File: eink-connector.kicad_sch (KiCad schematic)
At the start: 18 parts, among them J4 FFC-FPC_1X24_PIN, Q1 Si1308EDL

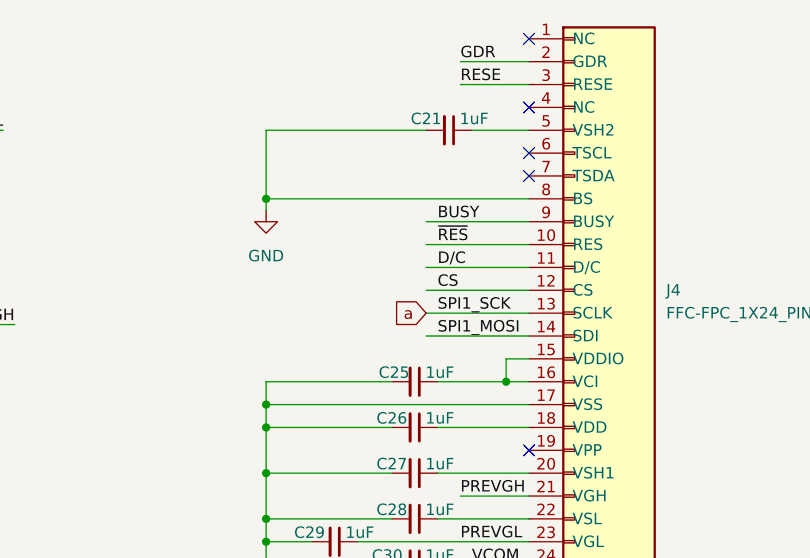
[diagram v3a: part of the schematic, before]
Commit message: Cleaned up local vs. global net labels
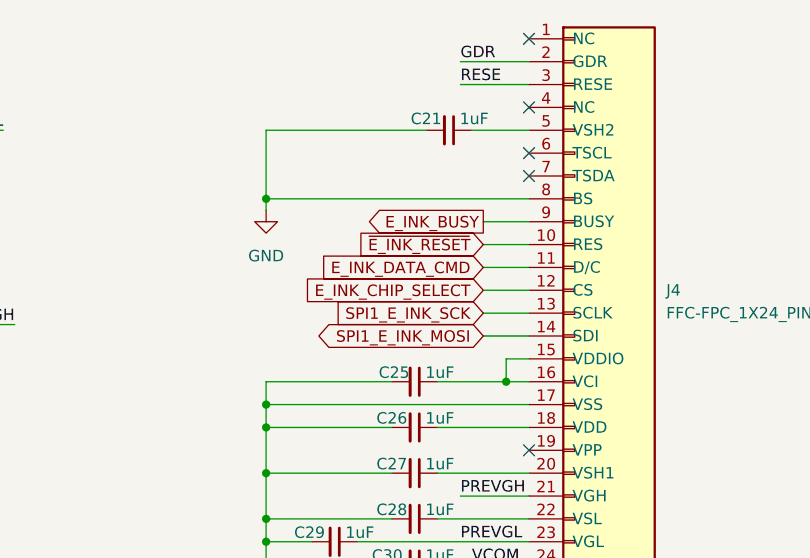
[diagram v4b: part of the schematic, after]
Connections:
- net BUSY renamed E_INK_BUSY
- net CS renamed E_INK_CHIP_SELECT
- net D/C renamed E_INK_DATA_CMD
- net SPI1_MOSI renamed SPI1_E_INK_MOSI
- net a renamed SPI1_E_INK_SCK
- net ~{RES} renamed ~{E_INK_RESET}
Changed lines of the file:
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@@
 	(wire
 		(pts
-			(xy 186.69 86.36) (xy 198.12 86.36)
+			(xy 193.04 86.36) (xy 198.12 86.36)
 		)
 		(stroke
@@
 	(wire
 		(pts
-			(xy 186.69 91.44) (xy 198.12 91.44)
+			(xy 193.04 91.44) (xy 198.12 91.44)
 		)
 		(stroke
@@
 	(wire
 		(pts
-			(xy 186.69 93.98) (xy 198.12 93.98)
+			(xy 193.04 93.98) (xy 198.12 93.98)
 		)
 		(stroke
@@
 	(wire
 		(pts
-			(xy 186.69 83.82) (xy 198.12 83.82)
+			(xy 193.04 83.82) (xy 198.12 83.82)
 		)
 		(stroke
@@
 	(wire
 		(pts
-			(xy 186.69 88.9) (xy 198.12 88.9)
-		)
-		(stroke
-			(width 0)
-			(type default)
-		)
-	)
-	(wire
-		(pts
-			(xy 186.69 96.52) (xy 198.12 96.52)
+			(xy 193.04 88.9) (xy 198.12 88.9)
+		)
+		(stroke
+			(width 0)
+			(type default)
+		)
+	)
+	(wire
+		(pts
+			(xy 193.04 96.52) (xy 198.12 96.52)
 		)
 		(stroke
@@
 		)
 	)
-	(label "SPI1_MOSI"
-		(at 187.96 96.52 0)
-		(effects
-			(font
-				(size 1.27 1.27)
-			)
-			(justify left bottom)
-		)
-	)
 	(label "PREVGH"
 		(at 140.97 95.25 180)
@@
 		)
 	)
-	(label "CS"
-		(at 187.96 91.44 0)
-		(effects
-			(font
-				(size 1.27 1.27)
-			)
-			(justify left bottom)
-		)
-	)
 	(label "GDR"
 		(at 190.5 66.04 0)
@@
 		)
 	)
-	(label "SPI1_SCK"
-		(at 187.96 93.98 0)
-		(effects
-			(font
-				(size 1.27 1.27)
-			)
-			(justify left bottom)
-		)
-	)
-	(label "BUSY"
-		(at 187.96 83.82 0)
-		(effects
-			(font
-				(size 1.27 1.27)
-			)
-			(justify left bottom)
-		)
-	)
-	(label "D{slash}C"
-		(at 187.96 88.9 0)
-		(effects
-			(font
-				(size 1.27 1.27)
-			)
-			(justify left bottom)
-		)
-	)
 	(label "RESE"
 		(at 118.11 114.3 180)
@@
 		)
 	)
-	(label "~{RES}"
-		(at 187.96 86.36 0)
-		(effects
-			(font
-				(size 1.27 1.27)
-			)
-			(justify left bottom)
-		)
-	)
-	(global_label "a"
+	(global_label "E_INK_DATA_CMD"
 		(shape input)
-		(at 186.69 93.98 180)
+		(at 193.04 88.9 180)
 		(fields_autoplaced yes)
 		(effects
@@
 		)
 		(property "Intersheetrefs" "${INTERSHEET_REFS}"
-			(at 182.5558 93.98 0)
+			(at 174.3915 88.9 0)
 			(effects
 				(font
+					(size 1.27 1.27)
+				)
+				(justify right)
+				(hide yes)
+			)
+		)
+	)
+	(global_label "E_INK_CHIP_SELECT"
+		(shape input)
+		(at 193.04 91.44 180)
+		(fields_autoplaced yes)
+		(effects
+			(font
+				(size 1.27 1.27)
+			)
+			(justify right)
+		)
+		(property "Intersheetrefs" "${INTERSHEET_REFS}"
+			(at 171.5492 91.44 0)
+			(effects
+				(font
+					(size 1.27 1.27)
+				)
+				(justify right)
+				(hide yes)
+			)
+		)
+	)
+	(global_label "E_INK_BUSY"
+		(shape output)
+		(at 193.04 83.82 180)
+		(fields_autoplaced yes)
+		(effects
+			(font
+				(size 1.27 1.27)
+			)
+			(justify right)
+		)
+		(property "Intersheetrefs" "${INTERSHEET_REFS}"
+			(at 178.8667 83.82 0)
+			(effects
+				(font
+					(size 1.27 1.27)
+				)
+				(justify right)
+				(hide yes)
+			)
+		)
+	)
+	(global_label "SPI1_E_INK_MOSI"
+		(shape bidirectional)
+		(at 193.04 96.52 180)
+		(fields_autoplaced yes)
+		(effects
+			(font
+				(size 1.27 1.27)
+			)
+			(justify right)
+		)
+		(property "Intersheetrefs" "${INTERSHEET_REFS}"
+			(at 172.7964 96.52 0)
+			(effects
+				(font
+					(size 1.27 1.27)
+				)
+				(justify right)
+				(hide yes)
+			)
+		)
+	)
+	(global_label "~{E_INK_RESET}"
+		(shape input)
+		(at 193.04 86.36 180)
+		(fields_autoplaced yes)
+		(effects
+			(font
+				(size 1.27 1.27)
+			)
+			(justify right)
+		)
+		(property "Intersheetrefs" "${INTERSHEET_REFS}"
+			(at 178.0202 86.36 0)
+			(effects
+				(font
+					(size 1.27 1.27)
+				)
+				(justify right)
+				(hide yes)
+			)
+		)
+	)
+	(global_label "SPI1_E_INK_SCK"
+		(shape input)
+		(at 193.04 93.98 180)
+		(fields_autoplaced yes)
+		(effects
+			(font
+				(size 1.27 1.27)
+			)
+			(justify right)
+		)
+		(property "Intersheetrefs" "${INTERSHEET_REFS}"
+			(at 174.7544 93.98 0)
+			(effects
+				(font

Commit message: ERC Check fixes
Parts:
- J4: symbol Connector_Generic:Conn_01x24 -> Connector_Generic:Conn_01x24_epaper_GDEM0122T61
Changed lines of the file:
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@@
 	)
 	(symbol
-		(lib_id "Connector_Generic:Conn_01x24")
+		(lib_id "Connector_Generic:Conn_01x24_epaper_GDEM0122T61")
 		(at 203.2 91.44 0)
 		(unit 1)

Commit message: Added test points and other cleanup
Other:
- note added: "Connector for GDEM0122T61 1.22 inch E-Ink display"
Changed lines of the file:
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@@
 	(generator_version "9.0")
 	(paper "A4")
+	(text "Connector for GDEM0122T61 1.22 inch E-Ink display"
+		(exclude_from_sim no)
+		(at 204.47 51.816 0)
+		(effects
+			(font
+				(size 2.032 2.032)
+			)
+		)
+	)
 	(junction
 		(at 168.91 104.14)

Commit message: changed fram for ic flash memory
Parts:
- R11, R12: footprint Resistor_SMD:R_0201_0603Metric -> Resistor_SMD:R_0603_1608Metric
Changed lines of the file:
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@@
 			)
 		)
-		(property "Description" "Unpolarized capacitor, small symbol"
+		(property "Description" "Unpolarized capacitor, small symbol, 0603/0805; X5R/X7R;Voltage Rating:≥25V"
 			(at 110.49 82.55 0)
 			(effects
@@
 			)
 		)
-		(property "Description" "Unpolarized capacitor, small symbol"
+		(property "Description" "Unpolarized capacitor, small symbol, 0603/0805; X5R/X7R;Voltage Rating:≥25V"
 			(at 185.42 121.92 0)
 			(effects
@@
 			)
 		)
-		(property "Description" "Unpolarized capacitor, small symbol"
+		(property "Description" "Unpolarized capacitor, small symbol, 0603/0805; X5R/X7R;Voltage Rating:≥25V"
 			(at 185.42 116.84 0)
 			(effects
@@
 			)
 		)
-		(property "Description" "Unpolarized capacitor, small symbol"
+		(property "Description" "Unpolarized capacitor, small symbol, 0603/0805; X5R/X7R;Voltage Rating:≥25V"
 			(at 185.42 106.68 0)
 			(effects
@@
 			)
 		)
-		(property "Description" "Unpolarized capacitor, small symbol"
+		(property "Description" "Unpolarized capacitor, small symbol, 0603/0805; X5R/X7R;Voltage Rating:≥25V"
 			(at 189.23 73.66 0)
 			(effects
@@
 			)
 		)
-		(property "Description" "Unpolarized capacitor, small symbol"
+		(property "Description" "Unpolarized capacitor, small symbol, , 0603/0805; X5R/X7R;Voltage Rating:≥25V"
 			(at 81.28 101.6 0)
 			(effects
@@
 			)
 		)
-		(property "Description" "Unpolarized capacitor, small symbol"
+		(property "Description" "Unpolarized capacitor, small symbol, 0603/0805; X5R/X7R;Voltage Rating:≥25V"
 			(at 176.53 119.38 0)
 			(effects
@@
 			)
 		)
-		(property "Description" "Unpolarized capacitor, small symbol"
+		(property "Description" "Unpolarized capacitor, small symbol, 0603/0805; X5R/X7R;Voltage Rating:≥25V"
 			(at 185.42 101.6 0)
 			(effects
@@
 			)
 		)
-		(property "Footprint" "Resistor_SMD:R_0201_0603Metric"
+		(property "Footprint" "Resistor_SMD:R_0603_1608Metric"
 			(at 108.712 121.92 90)
 			(effects
@@
 			)
 		)
-		(property "Description" "Resistor"
+		(property "Description" "Resistor, 0603/0805;1% variation,≥0.05W"
 			(at 110.49 121.92 0)
 			(effects
@@
 			)
 		)
-		(property "Description" "Unpolarized capacitor, small symbol"
+		(property "Description" "Unpolarized capacitor, small symbol, 0603/0805; X5R/X7R;Voltage Rating:≥25V"
 			(at 185.42 111.76 0)
 			(effects
@@
 			)
 		)
-		(property "Description" "Unpolarized capacitor, small symbol"
+		(property "Description" "Unpolarized capacitor, small symbol, 0603/0805; X5R/X7R;Voltage Rating:≥25V"
 			(at 132.08 101.6 0)
 			(effects
@@
 			)
 		)
-		(property "Footprint" "Resistor_SMD:R_0201_0603Metric"
+		(property "Footprint" "Resistor_SMD:R_0603_1608Metric"
 			(at 98.552 121.92 90)
 			(effects
@@
 			)
 		)
-		(property "Description" "Resistor"
+		(property "Description" "Resistor, 0603/0805;1% variation,≥0.05W"
 			(at 100.33 121.92 0)
 			(effects

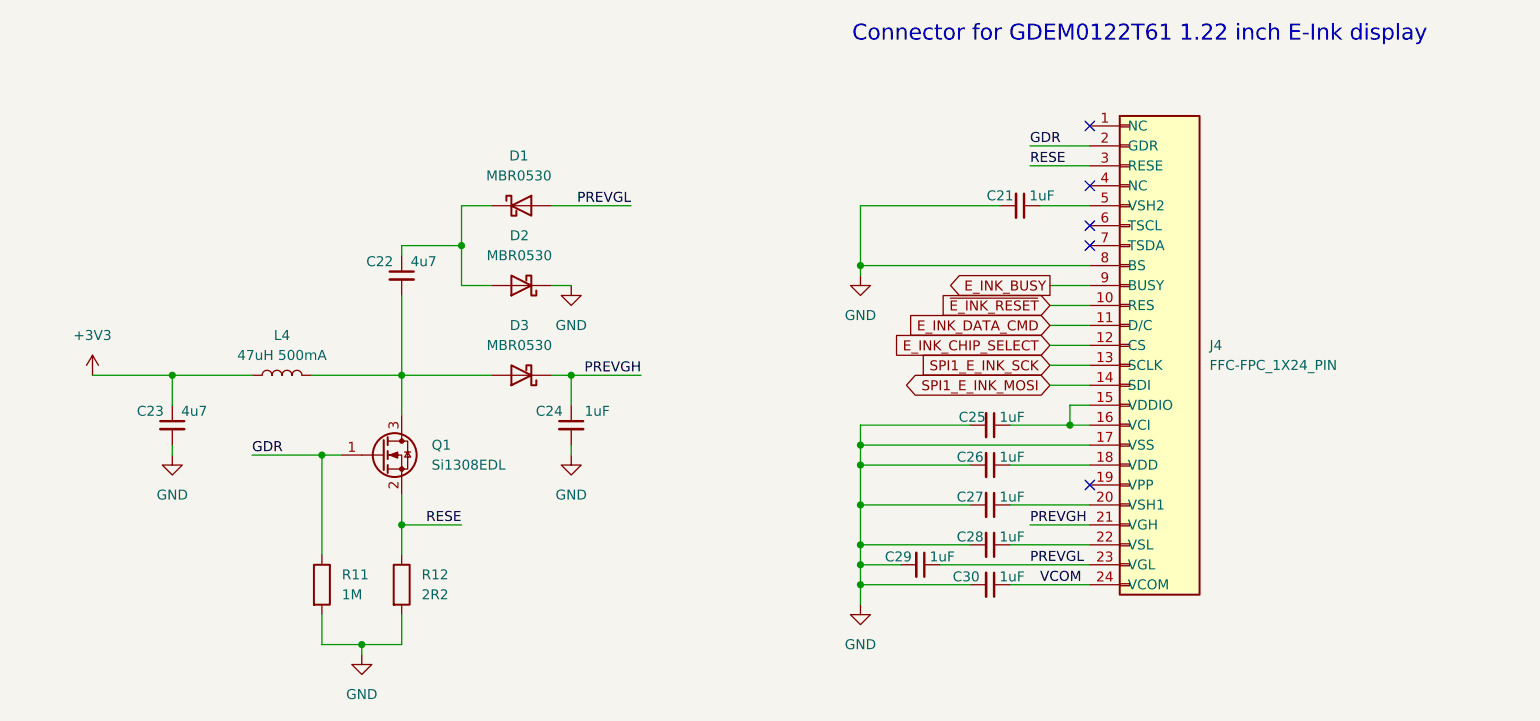
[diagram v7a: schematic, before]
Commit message: Choose footprints for all parts
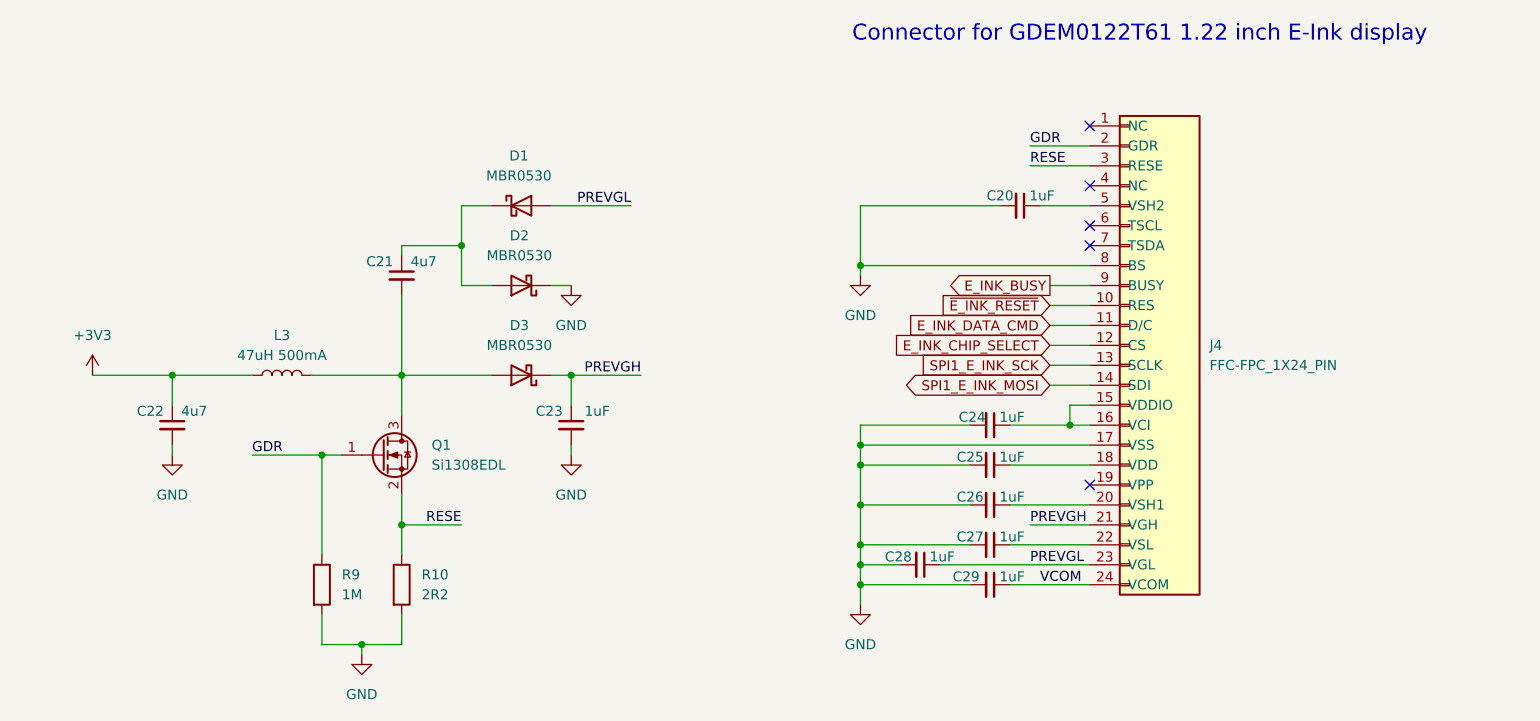
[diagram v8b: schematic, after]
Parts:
- L3: renamed from L4; footprint (none) -> Inductor_SMD:L_1210_3225Metric; MPN (none) -> ADL3225V-470MT-TL000
- renumbered C21 to C20, C22 to C21, C23 to C22, C24 to C23, C25 to C24, C26 to C25, C27 to C26, C28 to C27, C29 to C28, C30 to C29, R12 to R10, R11 to R9
